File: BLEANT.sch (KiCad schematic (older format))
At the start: 53 parts, among them IC1 FAN4010IL6X_F113, IC2 FAN4010IL6X_F113, J1 Conn_01x04_Male, J2 SC_19-20, J3 Conn_01x02, J4 Conn_01x02, J5 1909763-1, U1 nRF51x22-QFxx, U2 LM50BIM3, U3 MP5077GG-Z, U4 MP5077GG-Z, X2 32.768kHz, Y1 16MHz

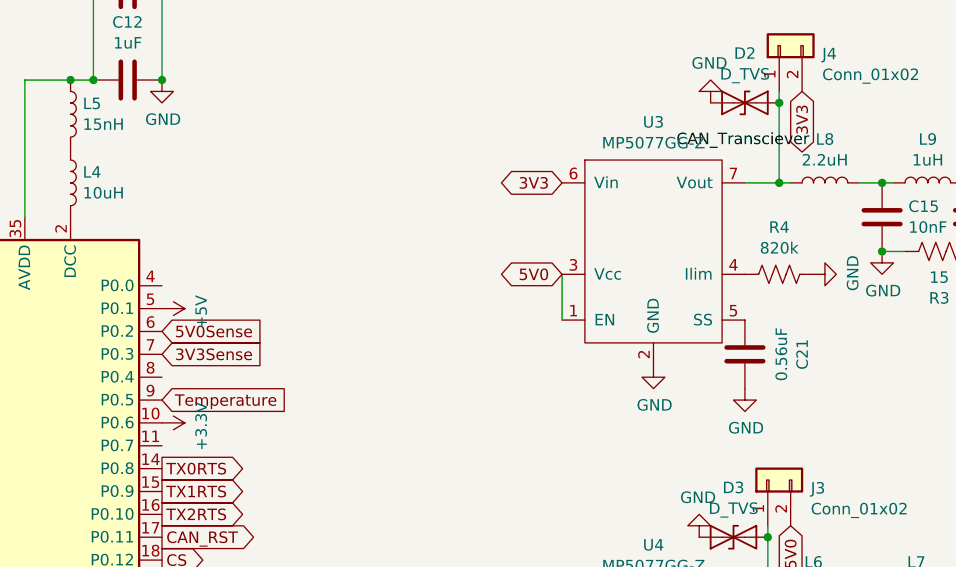
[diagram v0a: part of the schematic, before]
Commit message: Made my chip not blow up with voltage dividers
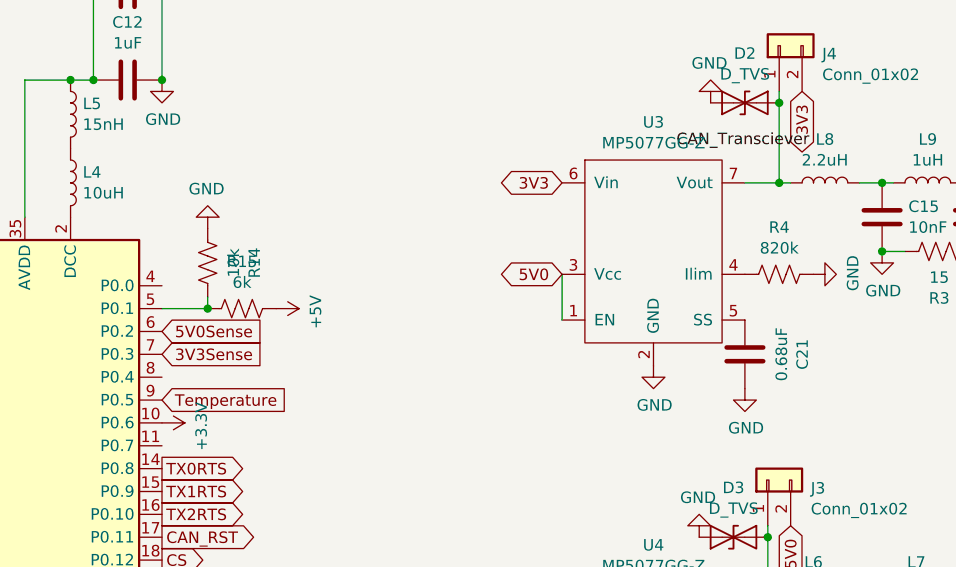
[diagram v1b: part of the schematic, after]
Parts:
- added R14: 10k, Resistor_SMD:R_0402_1005Metric, symbol Device:R_US
- added R15: 6k, Resistor_SMD:R_0402_1005Metric, symbol Device:R_US
- C21: value 0.56uF -> 0.68uF
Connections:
- wire segments 71 -> 73
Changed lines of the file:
@@
 P 7450 3200
 F 0 "C21" V 7198 3200 50  0000 C CNN
-F 1 "0.56uF" V 7289 3200 50  0000 C CNN
+F 1 "0.68uF" V 7289 3200 50  0000 C CNN
 F 2 "Capacitor_SMD:C_0402_1005Metric" H 7488 3050 50  0001 C CNN
 F 3 "~" H 7450 3200 50  0001 C CNN
@@
 L power:+5V #PWR0113
 U 1 1 5E3A5E8B
-P 4900 3000
-F 0 "#PWR0113" H 4900 2850 50  0001 C CNN
-F 1 "+5V" H 4915 3173 50  0000 C CNN
-F 2 "" H 4900 3000 50  0001 C CNN
-F 3 "" H 4900 3000 50  0001 C CNN
-	1    4900 3000
+P 5400 3000
+F 0 "#PWR0113" H 5400 2850 50  0001 C CNN
+F 1 "+5V" H 5415 3173 50  0000 C CNN
+F 2 "" H 5400 3000 50  0001 C CNN
+F 3 "" H 5400 3000 50  0001 C CNN
+	1    5400 3000
 	0    1    1    0
 $EndComp
@@
 Text GLabel 4900 4800 2    50   Input ~ 0
 RX1BF
+$Comp
+L Device:R_US R15
+U 1 1 5E08CFEF
+P 5250 3000
+F 0 "R15" V 5045 3000 50  0000 C CNN
+F 1 "6k" V 5136 3000 50  0000 C CNN
+F 2 "Resistor_SMD:R_0402_1005Metric" V 5290 2990 50  0001 C CNN
+F 3 "~" H 5250 3000 50  0001 C CNN
+	1    5250 3000
+	0    1    1    0
+$EndComp
+$Comp
+L Device:R_US R14
+U 1 1 5E08E68C
+P 5100 2800
+F 0 "R14" V 4895 2800 50  0000 C CNN
+F 1 "10k" V 4986 2800 50  0000 C CNN
+F 2 "Resistor_SMD:R_0402_1005Metric" V 5140 2790 50  0001 C CNN
+F 3 "~" H 5100 2800 50  0001 C CNN
+	1    5100 2800
+	-1   0    0    1
+$EndComp
+Wire Wire Line
+	4900 3000 5100 3000
+Wire Wire Line
+	5100 3000 5100 2950
+Connection ~ 5100 3000
+$Comp
+L power:GND #PWR0137
+U 1 1 5E092BC7
+P 5100 2650
+F 0 "#PWR0137" H 5100 2400 50  0001 C CNN
+F 1 "GND" H 5105 2477 50  0000 C CNN
+F 2 "" H 5100 2650 50  0001 C CNN
+F 3 "" H 5100 2650 50  0001 C CNN
+	1    5100 2650
+	-1   0    0    1
+$EndComp
 $EndSCHEMATC

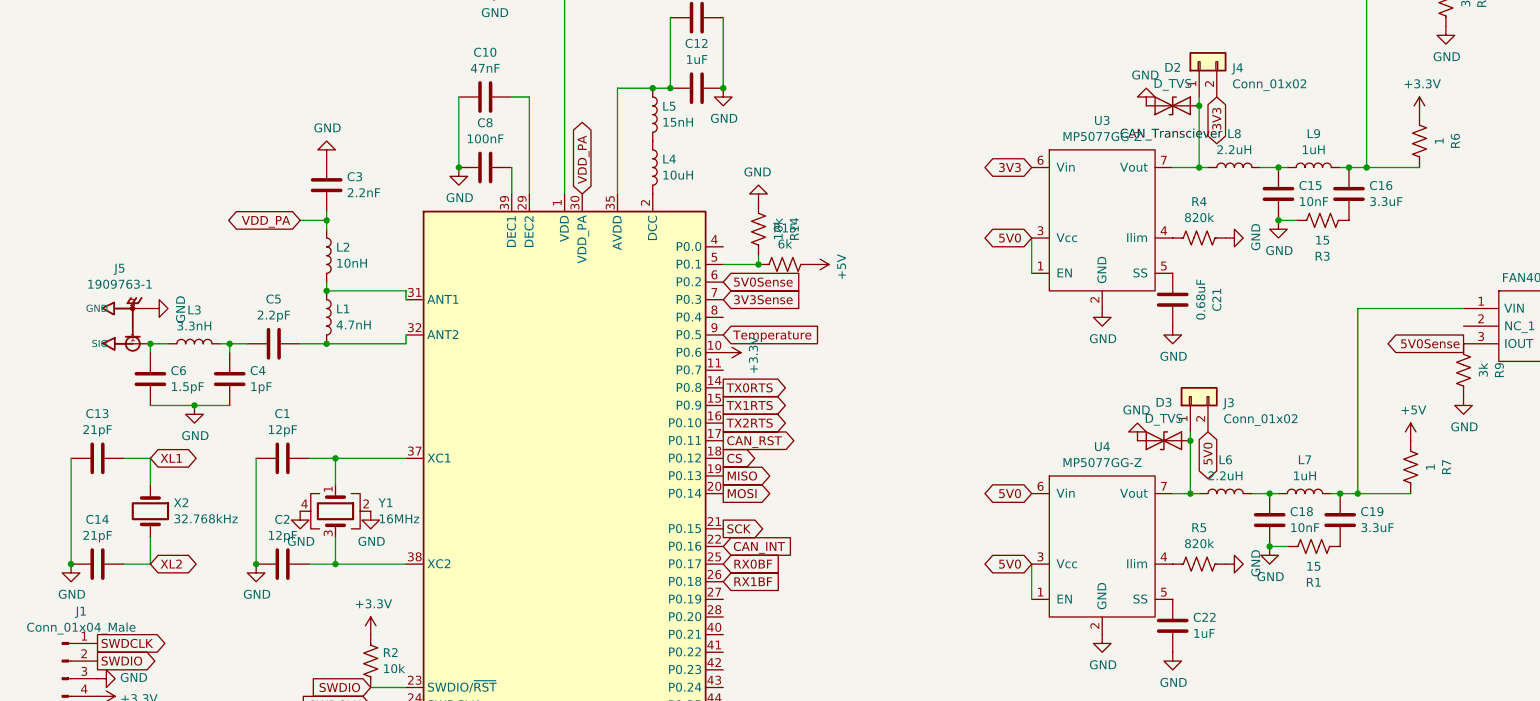
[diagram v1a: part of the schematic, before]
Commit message: Changed filter and fixed CAN circuit
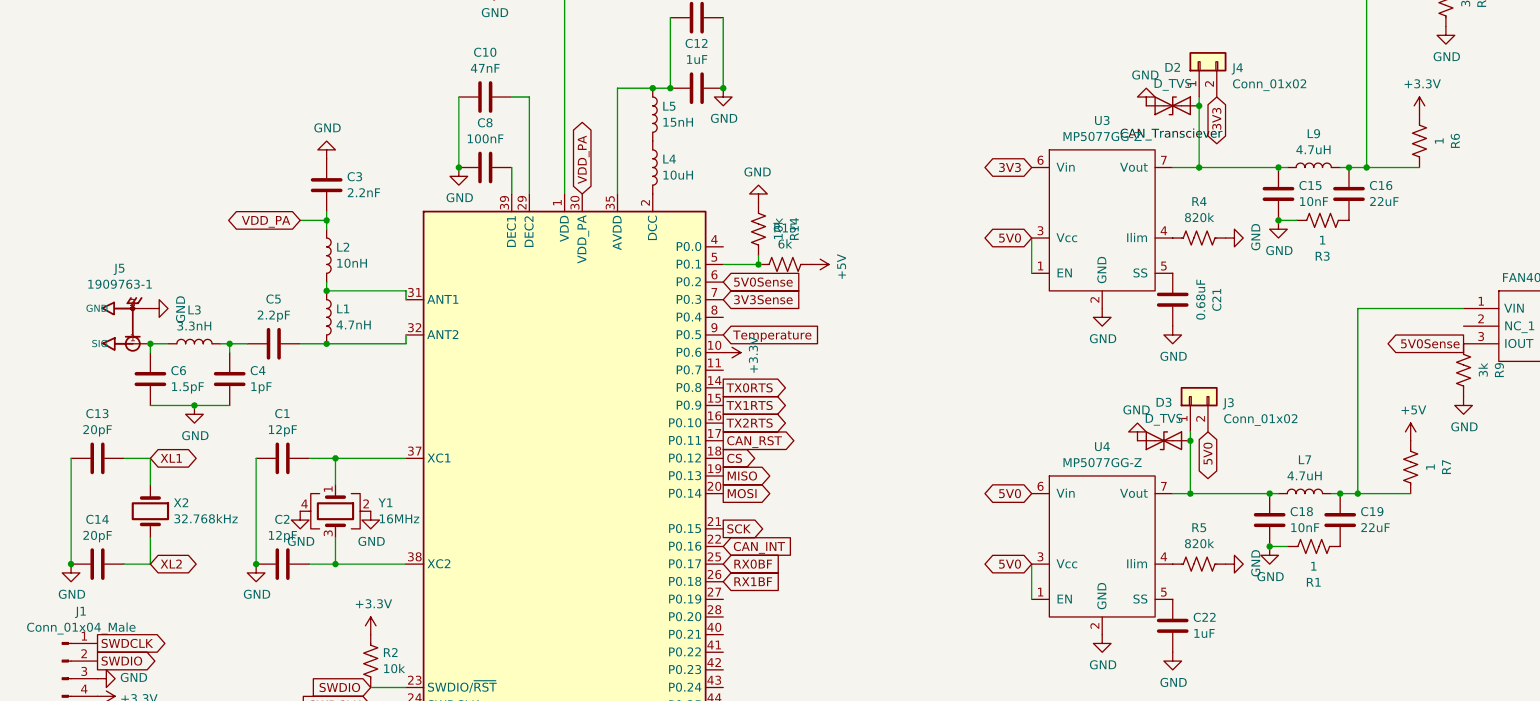
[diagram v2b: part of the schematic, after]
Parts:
- removed L6, L8: 2.2uH, Inductor_SMD:L_0402_1005Metric, symbol Device:L
- C13, C14: value 21pF -> 20pF
- C16, C19: value 3.3uF -> 22uF; footprint Capacitor_SMD:C_0402_1005Metric -> Capacitor_SMD:C_0805_2012Metric
- L7, L9: value 1uH -> 4.7uH; footprint Inductor_SMD:L_0402_1005Metric -> Inductor_SMD:L_0805_2012Metric
- R1, R3: value 15 -> 1
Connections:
- wire segments 73 -> 71
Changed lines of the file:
@@
 EESchema Schematic File Version 4
 LIBS:BLEANT-cache
+LIBS:CAN_Template-cache
 EELAYER 30 0
 EELAYER END
@@
 P 1350 4700
 F 0 "C14" V 1098 4700 50  0000 C CNN
-F 1 "21pF" V 1189 4700 50  0000 C CNN
+F 1 "20pF" V 1189 4700 50  0000 C CNN
 F 2 "Capacitor_SMD:C_0402_1005Metric" H 1388 4550 50  0001 C CNN
 F 3 "~" H 1350 4700 50  0001 C CNN
@@
 P 1350 4100
 F 0 "C13" V 1098 4100 50  0000 C CNN
-F 1 "21pF" V 1189 4100 50  0000 C CNN
+F 1 "20pF" V 1189 4100 50  0000 C CNN
 F 2 "Capacitor_SMD:C_0402_1005Metric" H 1388 3950 50  0001 C CNN
 F 3 "~" H 1350 4100 50  0001 C CNN
@@
 P 8400 4450
 F 0 "C19" H 8515 4496 50  0000 L CNN
-F 1 "3.3uF" H 8515 4405 50  0000 L CNN
-F 2 "Capacitor_SMD:C_0402_1005Metric" H 8438 4300 50  0001 C CNN
+F 1 "22uF" H 8515 4405 50  0000 L CNN
+F 2 "Capacitor_SMD:C_0805_2012Metric" H 8438 4300 50  0001 C CNN
 F 3 "~" H 8400 4450 50  0001 C CNN
 	1    8400 4450
@@
 P 8200 4300
 F 0 "L7" V 8390 4300 50  0000 C CNN
-F 1 "1uH" V 8299 4300 50  0000 C CNN
-F 2 "Inductor_SMD:L_0402_1005Metric" H 8200 4300 50  0001 C CNN
+F 1 "4.7uH" V 8299 4300 50  0000 C CNN
+F 2 "Inductor_SMD:L_0805_2012Metric" H 8200 4300 50  0001 C CNN
 F 3 "~" H 8200 4300 50  0001 C CNN
 	1    8200 4300
@@
 $EndComp
 Connection ~ 1650 3450
-$Comp
-L Device:L L6
-U 1 1 5E2AE530
-P 7750 4300
-F 0 "L6" V 7940 4300 50  0000 C CNN
-F 1 "2.2uH" V 7849 4300 50  0000 C CNN
-F 2 "Inductor_SMD:L_0402_1005Metric" H 7750 4300 50  0001 C CNN
-F 3 "~" H 7750 4300 50  0001 C CNN
-	1    7750 4300
-	0    -1   -1   0
-$EndComp
-Wire Wire Line
-	7600 4300 7550 4300
 Wire Wire Line
 	7550 3950 7550 4000
@@
 Wire Wire Line
 	7550 4300 7450 4300
-Wire Wire Line
-	7900 4300 8000 4300
 $Comp
 L Device:R_US R1
@@
 P 8250 4600
 F 0 "R1" V 8455 4600 50  0000 C CNN
-F 1 "15" V 8364 4600 50  0000 C CNN
+F 1 "1" V 8364 4600 50  0000 C CNN
 F 2 "Resistor_SMD:R_0402_1005Metric" V 8290 4590 50  0001 C CNN
 F 3 "~" H 8250 4600 50  0001 C CNN
@@
 Wire Wire Line
 	7550 4000 7550 4300
-Wire Wire Line
-	7650 2450 7600 2450
 Connection ~ 8550 2450
 Connection ~ 8450 2450
@@
 P 8450 2600
 F 0 "C16" H 8565 2646 50  0000 L CNN
-F 1 "3.3uF" H 8565 2555 50  0000 L CNN
-F 2 "Capacitor_SMD:C_0402_1005Metric" H 8488 2450 50  0001 C CNN
+F 1 "22uF" H 8565 2555 50  0000 L CNN
+F 2 "Capacitor_SMD:C_0805_2012Metric" H 8488 2450 50  0001 C CNN
 F 3 "~" H 8450 2600 50  0001 C CNN
 	1    8450 2600
@@
 P 8250 2450
 F 0 "L9" V 8440 2450 50  0000 C CNN
-F 1 "1uH" V 8349 2450 50  0000 C CNN
-F 2 "Inductor_SMD:L_0402_1005Metric" H 8250 2450 50  0001 C CNN
+F 1 "4.7uH" V 8349 2450 50  0000 C CNN
+F 2 "Inductor_SMD:L_0805_2012Metric" H 8250 2450 50  0001 C CNN
 F 3 "~" H 8250 2450 50  0001 C CNN
 	1    8250 2450
@@
 Connection ~ 8050 2450
 $Comp
-L Device:L L8
-U 1 1 5E2BA0AD
-P 7800 2450
-F 0 "L8" V 7990 2450 50  0000 C CNN
-F 1 "2.2uH" V 7899 2450 50  0000 C CNN
-F 2 "Inductor_SMD:L_0402_1005Metric" H 7800 2450 50  0001 C CNN
-F 3 "~" H 7800 2450 50  0001 C CNN
-	1    7800 2450
-	0    -1   -1   0
-$EndComp
-Wire Wire Line
-	7950 2450 8050 2450
-$Comp
 L Device:R_US R3
 U 1 1 5E2BA0B9
 P 8300 2750
 F 0 "R3" V 8505 2750 50  0000 C CNN
-F 1 "15" V 8414 2750 50  0000 C CNN
+F 1 "1" V 8414 2750 50  0000 C CNN
 F 2 "Resistor_SMD:R_0402_1005Metric" V 8340 2740 50  0001 C CNN
 F 3 "~" H 8300 2750 50  0001 C CNN
@@
 	-1   0    0    1
 $EndComp
+Wire Wire Line
+	7550 4300 8000 4300
+Wire Wire Line
+	7600 2450 8050 2450
 $EndSCHEMATC

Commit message: Added filters and decoupling caps to temp sensor. Fixed pullup/down resistors on SWD
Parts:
- added C31, C33: 1nF, Capacitor_SMD:C_0402_1005Metric, symbol Device:C
- added C32, C34, C35: 100nF, Capacitor_SMD:C_0402_1005Metric, symbol Device:C
- added C36: 2.2uF, Capacitor_SMD:C_0402_1005Metric, symbol Device:C
- added L6: 2.2uH, Inductor_SMD:L_0402_1005Metric, symbol Device:L
- added R17: 3.3k, Resistor_SMD:R_0402_1005Metric, symbol Device:R_US
- added R18: 3.3, Resistor_SMD:R_0402_1005Metric, symbol Device:R_US
- R2: value 10k -> 1k
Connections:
- wire segments 71 -> 87

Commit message: Added the filter and other alterations to routing. Removed copper peninsulas and improved routing overall
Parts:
- removed U2: LM50BIM3, footprints:LM50_DBZ_3, symbol 2019-12-19_22-46-35:LM50BIM3
- added TMP1: LM50CIM3X, Package_TO_SOT_SMD:SOT-23, symbol MASA_Library:LM50CIM3X
- IC1, IC2: footprint FAN4010:6-LEAD_MICROPAK -> MASA_Library:6-LEAD_MICROPAK
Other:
- moved on the sheet: C33, C34, C35, C36, L6, R17, R18
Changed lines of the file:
@@
 L power:GND #PWR0115
 U 1 1 5DFC480D
-P 13450 1050
-F 0 "#PWR0115" H 13450 800 50  0001 C CNN
-F 1 "GND" V 13455 922 50  0000 R CNN
-F 2 "" H 13450 1050 50  0001 C CNN
-F 3 "" H 13450 1050 50  0001 C CNN
-	1    13450 1050
-	0    -1   -1   0
+P 11950 1300
+F 0 "#PWR0115" H 11950 1050 50  0001 C CNN
+F 1 "GND" V 11955 1172 50  0000 R CNN
+F 2 "" H 11950 1300 50  0001 C CNN
+F 3 "" H 11950 1300 50  0001 C CNN
+	1    11950 1300
+	1    0    0    -1
 $EndComp
 $Comp
@@
 	0    -1   -1   0
 $EndComp
-Text GLabel 15300 1150 2    50   Output ~ 0
+Text GLabel 14200 1050 2    50   Output ~ 0
 Temperature
 $Comp
@@
 $EndComp
 $Comp
-L 2019-12-19_22-46-35:LM50BIM3 U2
-U 1 1 5DFFA48C
-P 11250 1050
-F 0 "U2" H 12350 1437 60  0000 C CNN
-F 1 "LM50BIM3" H 12350 1331 60  0000 C CNN
-F 2 "footprints:LM50_DBZ_3" H 12350 1290 60  0001 C CNN
-F 3 "" H 11250 1050 60  0000 C CNN
-	1    11250 1050
-	1    0    0    -1
-$EndComp
-$Comp
 L power:GND #PWR0127
 U 1 1 5DFEE4BE
@@
 F 0 "IC1" H 9550 1415 50  0000 C CNN
 F 1 "FAN4010IL6X_F113" H 9550 1324 50  0000 C CNN
-F 2 "FAN4010:6-LEAD_MICROPAK" H 9950 1250 50  0001 L CNN
+F 2 "MASA_Library:6-LEAD_MICROPAK" H 9950 1250 50  0001 L CNN
 F 3 "http://pdl.designspark.com/api/v1/manufacturers/53f31bb99b4759f8698ebd6d/part/54f601839b4759c27e8ce92c/54f601849b4759c27e8ce954/1pdf" H 9950 1150 50  0001 L CNN
 F 4 "Current Sense Amplifier Single Single Ended 6-Pin MLP" H 9950 1050 50  0001 L CNN "Description"
@@
 F 0 "IC2" H 9650 3515 50  0000 C CNN
 F 1 "FAN4010IL6X_F113" H 9650 3424 50  0000 C CNN
-F 2 "FAN4010:6-LEAD_MICROPAK" H 10050 3350 50  0001 L CNN
+F 2 "MASA_Library:6-LEAD_MICROPAK" H 10050 3350 50  0001 L CNN
 F 3 "http://pdl.designspark.com/api/v1/manufacturers/53f31bb99b4759f8698ebd6d/part/54f601839b4759c27e8ce92c/54f601849b4759c27e8ce954/1pdf" H 10050 3250 50  0001 L CNN
 F 4 "Current Sense Amplifier Single Single Ended 6-Pin MLP" H 10050 3150 50  0001 L CNN "Description"
@@
 	1    0    0    -1
 $EndComp
-Wire Wire Line
-	11250 1050 11200 1050
 Connection ~ 10800 1050
 Connection ~ 11200 1050
@@
 L Device:C C33
 U 1 1 5E22CAA1
-P 13550 1300
-F 0 "C33" H 13665 1346 50  0000 L CNN
-F 1 "1nF" H 13665 1255 50  0000 L CNN
-F 2 "Capacitor_SMD:C_0402_1005Metric" H 13588 1150 50  0001 C CNN
-F 3 "~" H 13550 1300 50  0001 C CNN
-	1    13550 1300
+P 12450 1200
+F 0 "C33" H 12565 1246 50  0000 L CNN
+F 1 "1nF" H 12565 1155 50  0000 L CNN
+F 2 "Capacitor_SMD:C_0402_1005Metric" H 12488 1050 50  0001 C CNN
+F 3 "~" H 12450 1200 50  0001 C CNN
+	1    12450 1200
 	1    0    0    -1
 $EndComp
@@
 L Device:C C34
 U 1 1 5E22D031
-P 13950 1300
-F 0 "C34" H 14065 1346 50  0000 L CNN
-F 1 "100nF" H 14065 1255 50  0000 L CNN
-F 2 "Capacitor_SMD:C_0402_1005Metric" H 13988 1150 50  0001 C CNN
-F 3 "~" H 13950 1300 50  0001 C CNN
-	1    13950 1300
+P 12850 1200
+F 0 "C34" H 12965 1246 50  0000 L CNN
+F 1 "100nF" H 12965 1155 50  0000 L CNN
+F 2 "Capacitor_SMD:C_0402_1005Metric" H 12888 1050 50  0001 C CNN
+F 3 "~" H 12850 1200 50  0001 C CNN
+	1    12850 1200
 	1    0    0    -1
 $EndComp
@@
 L Device:R_US R17
 U 1 1 5E22D409
-P 14300 1300
-F 0 "R17" V 14505 1300 50  0000 C CNN
-F 1 "3.3k" V 14414 1300 50  0000 C CNN
-F 2 "Resistor_SMD:R_0402_1005Metric" V 14340 1290 50  0001 C CNN
-F 3 "~" H 14300 1300 50  0001 C CNN
-	1    14300 1300
+P 13200 1200
+F 0 "R17" V 13405 1200 50  0000 C CNN
+F 1 "3.3k" V 13314 1200 50  0000 C CNN
+F 2 "Resistor_SMD:R_0402_1005Metric" V 13240 1190 50  0001 C CNN
+F 3 "~" H 13200 1200 50  0001 C CNN
+	1    13200 1200
 	1    0    0    -1
 $EndComp
@@
 L Device:L L6
 U 1 1 5E22DD66
-P 14600 1150
-F 0 "L6" V 14790 1150 50  0000 C CNN
-F 1 "2.2uH" V 14699 1150 50  0000 C CNN
-F 2 "Inductor_SMD:L_0402_1005Metric" H 14600 1150 50  0001 C CNN
-F 3 "~" H 14600 1150 50  0001 C CNN
-	1    14600 1150
+P 13500 1050
+F 0 "L6" V 13690 1050 50  0000 C CNN
+F 1 "2.2uH" V 13599 1050 50  0000 C CNN
+F 2 "Inductor_SMD:L_0402_1005Metric" H 13500 1050 50  0001 C CNN
+F 3 "~" H 13500 1050 50  0001 C CNN
+	1    13500 1050
 	0    -1   -1   0
 $EndComp
@@
 L Device:C C35
 U 1 1 5E22E43E
-P 14850 1300
-F 0 "C35" H 14965 1346 50  0000 L CNN
-F 1 "100nF" H 14965 1255 50  0000 L CNN
-F 2 "Capacitor_SMD:C_0402_1005Metric" H 14888 1150 50  0001 C CNN
-F 3 "~" H 14850 1300 50  0001 C CNN
-	1    14850 1300
+P 13750 1200
+F 0 "C35" H 13865 1246 50  0000 L CNN
+F 1 "100nF" H 13865 1155 50  0000 L CNN
+F 2 "Capacitor_SMD:C_0402_1005Metric" H 13788 1050 50  0001 C CNN
+F 3 "~" H 13750 1200 50  0001 C CNN
+	1    13750 1200
 	1    0    0    -1
 $EndComp
@@
 L Device:C C36
 U 1 1 5E22E6DF
-P 15250 1300
-F 0 "C36" H 15365 1346 50  0000 L CNN
-F 1 "2.2uF" H 15365 1255 50  0000 L CNN
-F 2 "Capacitor_SMD:C_0402_1005Metric" H 15288 1150 50  0001 C CNN
-F 3 "~" H 15250 1300 50  0001 C CNN
-	1    15250 1300
+P 14150 1200
+F 0 "C36" H 14265 1246 50  0000 L CNN
+F 1 "2.2uF" H 14265 1155 50  0000 L CNN
+F 2 "Capacitor_SMD:C_0402_1005Metric" H 14188 1050 50  0001 C CNN
+F 3 "~" H 14150 1200 50  0001 C CNN
+	1    14150 1200
 	1    0    0    -1
 $EndComp
@@
 L Device:R_US R18
 U 1 1 5E22EAC4
-P 15050 1450
-F 0 "R18" V 15255 1450 50  0000 C CNN
-F 1 "3.3" V 15164 1450 50  0000 C CNN
-F 2 "Resistor_SMD:R_0402_1005Metric" V 15090 1440 50  0001 C CNN
-F 3 "~" H 15050 1450 50  0001 C CNN
-	1    15050 1450
-	0    1    1    0
-$EndComp
-Wire Wire Line
-	15300 1150 15250 1150
-Connection ~ 14850 1150
-Wire Wire Line
-	14850 1150 14750 1150
-Connection ~ 15250 1150
-Wire Wire Line
-	15250 1150 14850 1150
-Wire Wire Line
-	14450 1150 14300 1150
-Connection ~ 13550 1150
-Wire Wire Line
-	13550 1150 13450 1150
-Connection ~ 13950 1150
-Wire Wire Line
-	13950 1150 13550 1150
-Connection ~ 14300 1150
-Wire Wire Line
-	14300 1150 13950 1150
-Wire Wire Line
-	13550 1450 13950 1450
-Connection ~ 13950 1450
-Wire Wire Line
-	13950 1450 14300 1450
-Wire Wire Line
-	14850 1450 14900 1450
-Wire Wire Line
-	15200 1450 15250 1450
+P 13950 1350
+F 0 "R18" V 14155 1350 50  0000 C CNN
+F 1 "3.3" V 14064 1350 50  0000 C CNN
+F 2 "Resistor_SMD:R_0402_1005Metric" V 13990 1340 50  0001 C CNN
+F 3 "~" H 13950 1350 50  0001 C CNN
+	1    13950 1350
+	0    1    1    0
+$EndComp
+Wire Wire Line
+	14200 1050 14150 1050
+Connection ~ 13750 1050
+Wire Wire Line
+	13750 1050 13650 1050
+Connection ~ 14150 1050
+Wire Wire Line
+	14150 1050 13750 1050
+Wire Wire Line
+	13350 1050 13200 1050
+Connection ~ 12450 1050
+Wire Wire Line
+	12450 1050 12350 1050
+Connection ~ 12850 1050
+Wire Wire Line
+	12850 1050 12450 1050
+Connection ~ 13200 1050
+Wire Wire Line
+	13200 1050 12850 1050
+Wire Wire Line
+	12450 1350 12850 1350
+Connection ~ 12850 1350
+Wire Wire Line
+	12850 1350 13200 1350
+Wire Wire Line
+	13750 1350 13800 1350
+Wire Wire Line
+	14100 1350 14150 1350
 $Comp
 L power:GND #PWR031
 U 1 1 5E23A175
-P 13950 1450
-F 0 "#PWR031" H 13950 1200 50  0001 C CNN
-F 1 "GND" H 13955 1277 50  0000 C CNN
-F 2 "" H 13950 1450 50  0001 C CNN
-F 3 "" H 13950 1450 50  0001 C CNN
-	1    13950 1450
+P 12850 1350
+F 0 "#PWR031" H 12850 1100 50  0001 C CNN
+F 1 "GND" H 12855 1177 50  0000 C CNN
+F 2 "" H 12850 1350 50  0001 C CNN
+F 3 "" H 12850 1350 50  0001 C CNN
+	1    12850 1350
 	1    0    0    -1
 $EndComp
@@
 L power:GND #PWR032
 U 1 1 5E23A751
-P 14850 1450
-F 0 "#PWR032" H 14850 1200 50  0001 C CNN
-F 1 "GND" H 14855 1277 50  0000 C CNN
-F 2 "" H 14850 1450 50  0001 C CNN
-F 3 "" H 14850 1450 50  0001 C CNN
-	1    14850 1450
-	1    0    0    -1
-$EndComp
-Connection ~ 14850 1450
+P 13750 1350
+F 0 "#PWR032" H 13750 1100 50  0001 C CNN
+F 1 "GND" H 13755 1177 50  0000 C CNN
+F 2 "" H 13750 1350 50  0001 C CNN
+F 3 "" H 13750 1350 50  0001 C CNN
+	1    13750 1350
+	1    0    0    -1
+$EndComp
+Connection ~ 13750 1350
 $Comp
 L Device:R_US R2
@@
 	1    0    0    -1
 $EndComp
+$Comp
+L MASA_Library:LM50CIM3X TMP1
+U 1 1 5E24F61B
+P 11950 1050
+F 0 "TMP1" H 11950 1365 50  0000 C CNN
+F 1 "LM50CIM3X" H 11950 1274 50  0000 C CNN
+F 2 "Package_TO_SOT_SMD:SOT-23" H 11950 1300 50  0001 C CNN
+F 3 "" H 11950 1300 50  0001 C CNN
+	1    11950 1050
+	1    0    0    -1
+$EndComp
+Wire Wire Line
+	11200 1050 11550 1050
 $EndSCHEMATC
